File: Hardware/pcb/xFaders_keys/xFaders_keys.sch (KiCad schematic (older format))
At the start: 76 parts, among them J1 Conn_02x10_Odd_Even, SW1 SW_Push, SW10 SW_Push, SW11 SW_Push, SW12 SW_Push, SW13 SW_Push, SW14 SW_Push, SW15 SW_Push, SW16 SW_Push, SW17 SW_Push, SW18 SW_Push, SW19 SW_Push, SW2 SW_Push, SW20 SW_Push, SW21 SW_Push, SW22 SW_Push, SW23 SW_Push, SW24 SW_Push, SW25 SW_Push, SW26 SW_Push, SW27 SW_Push, SW28 SW_Push, SW29 SW_Push, SW3 SW_Push, SW30 SW_Push, SW31 SW_Push, SW32 SW_Push, SW33 SW_Push, SW34 SW_Push, SW35 SW_Push, SW36 SW_Push, SW37 SW_Push, SW38 SW_Push, SW39 SW_Push, SW4 SW_Push, SW40 SW_Push, SW41 SW_Push, SW42 SW_Push, SW43 SW_Push, SW44 SW_Push, SW45 SW_Push, SW5 SW_Push, SW6 SW_Push, SW7 SW_Push, SW8 SW_Push, SW9 SW_Push

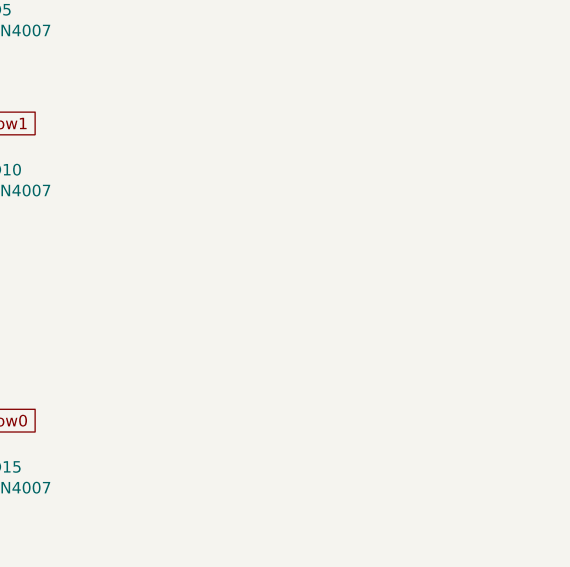
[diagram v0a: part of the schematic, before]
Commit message: Add kicad library for SK6812 MINI-E RGB LEDs
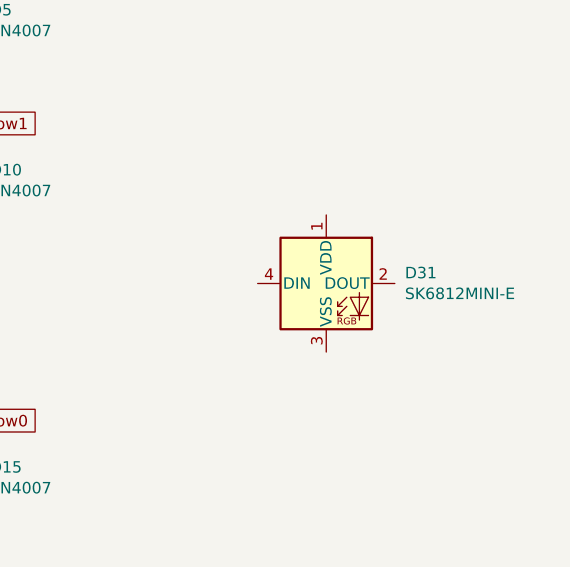
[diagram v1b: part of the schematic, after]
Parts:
- added D31: SK6812MINI-E, kicad-keyboard-parts:MX_SK6812MINI-E, symbol kicad-keyboard-parts:SK6812MINI-E
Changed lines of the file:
@@
 EESchema Schematic File Version 4
-LIBS:xFaders_keys-cache
 EELAYER 30 0
 EELAYER END
@@
 Wire Wire Line
 	6900 6000 6900 5900
+$Comp
+L kicad-keyboard-parts:SK6812MINI-E D31
+U 1 1 6025F252
+P 8450 2500
+F 0 "D31" H 8794 2546 50  0000 L CNN
+F 1 "SK6812MINI-E" H 8794 2455 50  0000 L CNN
+F 2 "kicad-keyboard-parts:MX_SK6812MINI-E" H 8500 2200 50  0001 L TNN
+F 3 "https://cdn-shop.adafruit.com/product-files/2686/SK6812MINI_REV.01-1-2.pdf" H 8550 2125 50  0001 L TNN
+	1    8450 2500
+	1    0    0    -1
+$EndComp
 $EndSCHEMATC

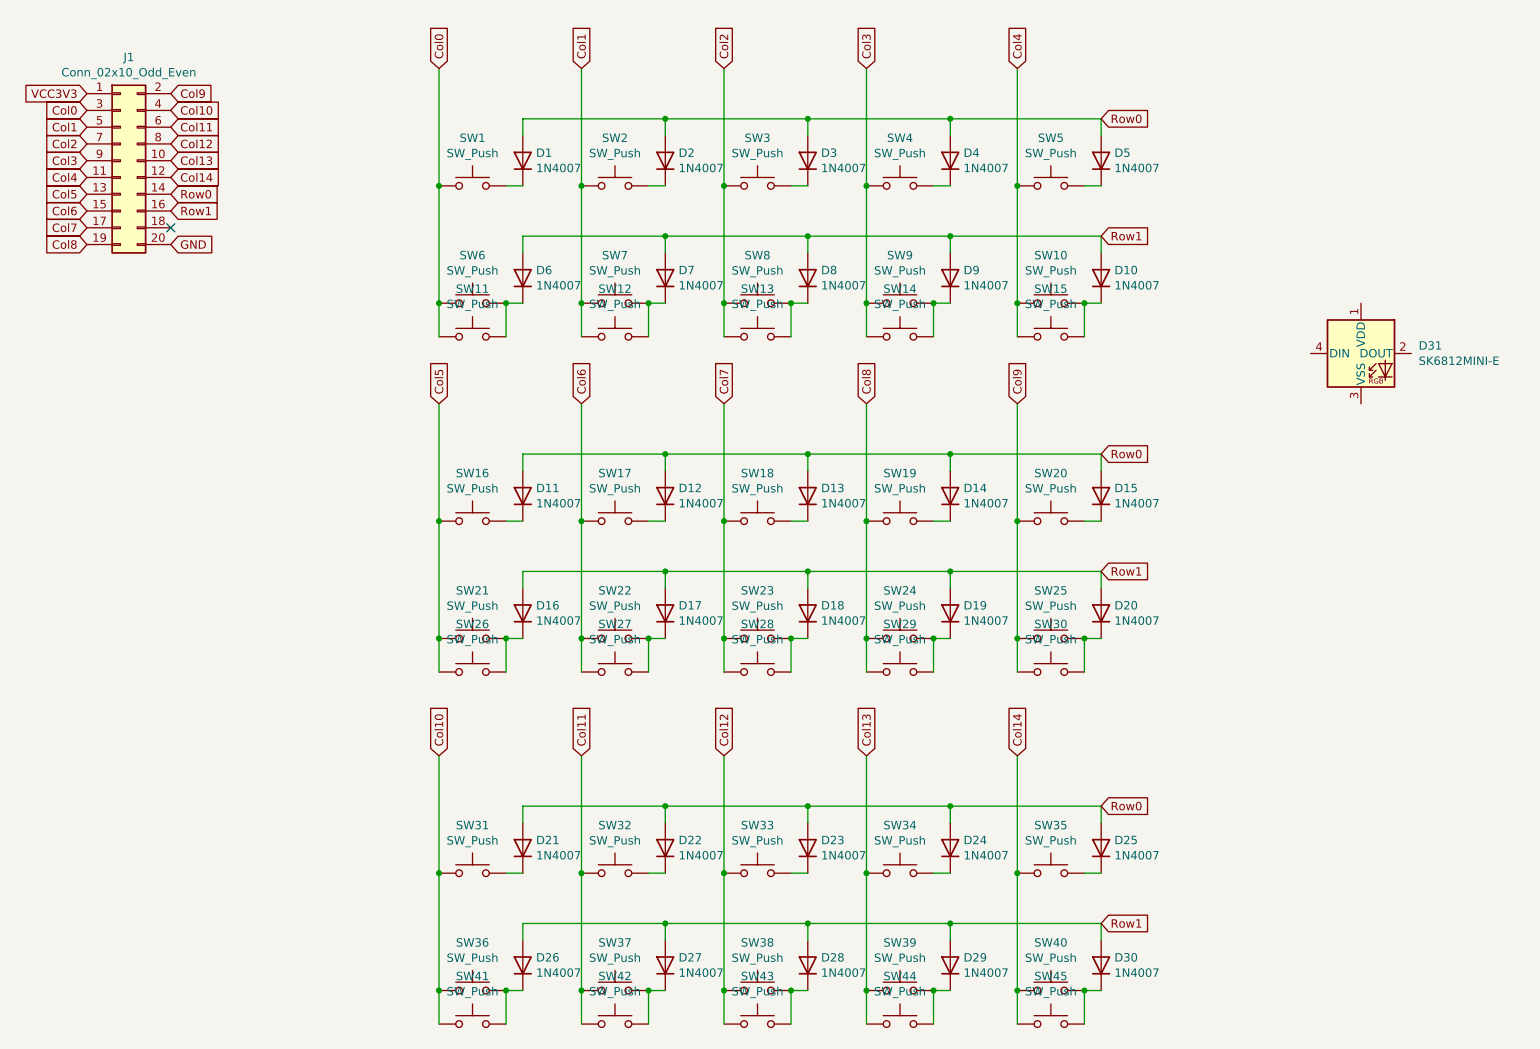
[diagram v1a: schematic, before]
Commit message: Add RGB LEDs and capacitors to Schema and PCB
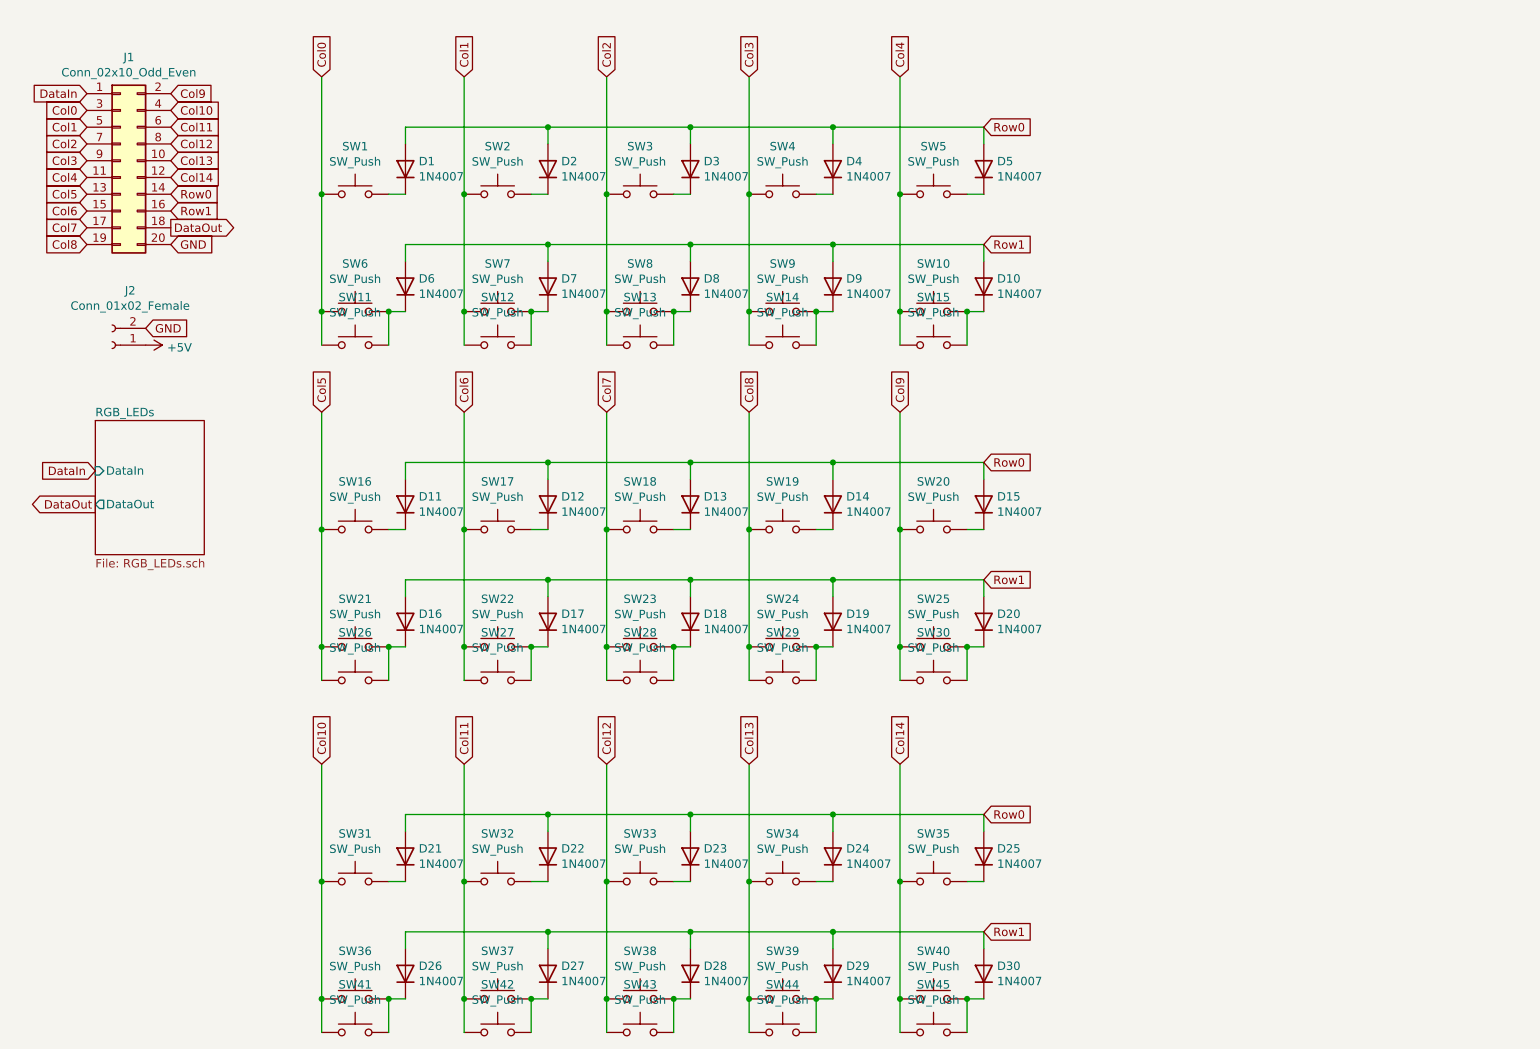
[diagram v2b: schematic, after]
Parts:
- removed D31: SK6812MINI-E, kicad-keyboard-parts:MX_SK6812MINI-E, symbol kicad-keyboard-parts:SK6812MINI-E
- added J2: Conn_01x02_Female, Connector_PinHeader_2.54mm:PinHeader_1x02_P2.54mm_Vertical, symbol Connector:Conn_01x02_Female
- D1, D10, D11, D12, D13, D14, D15, D16, D17, D18, D19, D2, D20, D21, D22, D23, D24, D25, D26, D27, D28, D29, D3, D30, D4, D5, D6, D7, D8, D9: footprint Diode_THT:D_DO-41_SOD81_P10.16mm_Horizontal -> Diode_THT:D_DO-35_SOD27_P10.16mm_Horizontal
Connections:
- net GND: now also J2.2 (Pin_2)
- net DataOut: now reaches J1.18 (Pin_18)
- net VCC3V3 renamed DataIn
- new net +5V: J2.1 (Pin_1)
- no-connect marks 1 -> 0
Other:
- moved on the sheet: D1, D10, D11, D12, D13, D14, D15, D16, D17, D18, D19, D2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

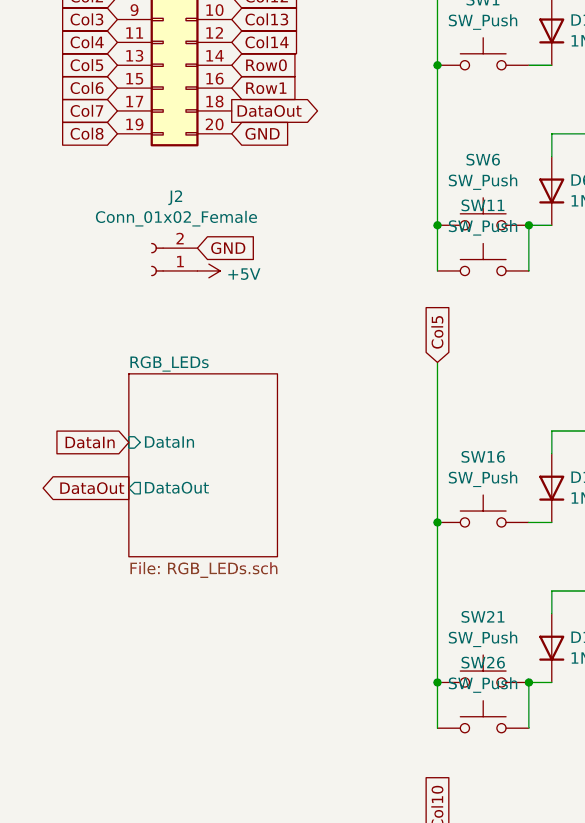
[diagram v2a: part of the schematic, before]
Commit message: Update PCB for new RGB LEDs and 5V power supply
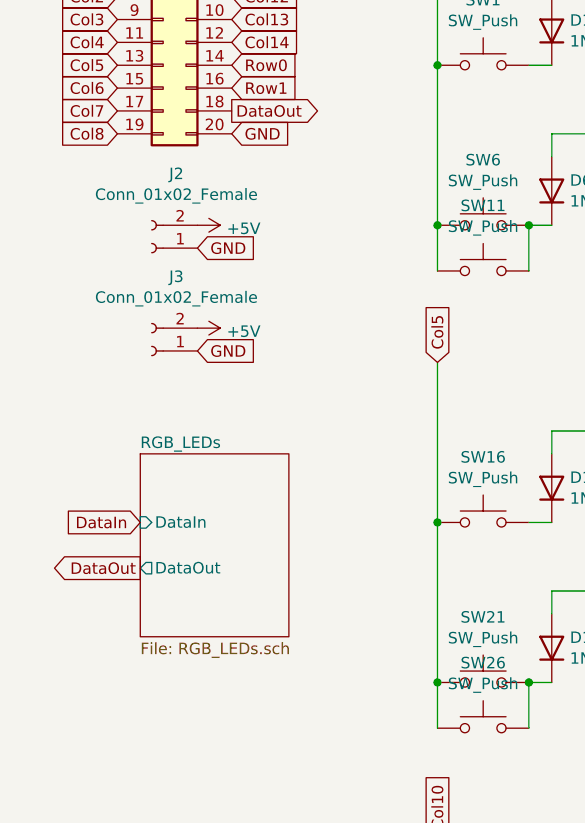
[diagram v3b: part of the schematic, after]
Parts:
- added J3: Conn_01x02_Female, Connector_PinHeader_2.54mm:PinHeader_1x02_P2.54mm_Vertical, symbol Connector:Conn_01x02_Female
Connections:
- net +5V: now also J2.2 (Pin_2), J3.2 (Pin_2); no longer J2.1 (Pin_1)
- net GND: now also J2.1 (Pin_1), J3.1 (Pin_1); no longer J2.2 (Pin_2)
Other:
- moved on the sheet: J2
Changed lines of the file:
@@
 Wire Wire Line
 	6200 6050 6200 5950
-$Sheet
-S 900  2900 650  800
-U 602D74FD
-F0 "RGB_LEDs" 50
-F1 "RGB_LEDs.sch" 50
-F2 "DataIn" I L 900 3200 50
-F3 "DataOut" O L 900 3400 50
-$EndSheet
 $Comp
 L Connector:Conn_01x02_Female J2
 U 1 1 605C87E4
-P 1000 2450
-F 0 "J2" H 892 2125 50  0000 C CNN
-F 1 "Conn_01x02_Female" H 892 2216 50  0000 C CNN
-F 2 "Connector_PinHeader_2.54mm:PinHeader_1x02_P2.54mm_Vertical" H 1000 2450 50  0001 C CNN
-F 3 "~" H 1000 2450 50  0001 C CNN
-	1    1000 2450
+P 1000 2350
+F 0 "J2" H 892 2025 50  0000 C CNN
+F 1 "Conn_01x02_Female" H 892 2116 50  0000 C CNN
+F 2 "Connector_PinHeader_2.54mm:PinHeader_1x02_P2.54mm_Vertical" H 1000 2350 50  0001 C CNN
+F 3 "~" H 1000 2350 50  0001 C CNN
+	1    1000 2350
 	-1   0    0    1
 $EndComp
@@
 L power:+5V #PWR025
 U 1 1 605CA370
-P 1200 2450
-F 0 "#PWR025" H 1200 2300 50  0001 C CNN
-F 1 "+5V" V 1215 2578 50  0000 L CNN
-F 2 "" H 1200 2450 50  0001 C CNN
-F 3 "" H 1200 2450 50  0001 C CNN
-	1    1200 2450
+P 1200 2250
+F 0 "#PWR025" H 1200 2100 50  0001 C CNN
+F 1 "+5V" V 1215 2378 50  0000 L CNN
+F 2 "" H 1200 2250 50  0001 C CNN
+F 3 "" H 1200 2250 50  0001 C CNN
+	1    1200 2250
 	0    1    1    0
 $EndComp
@@
 Text GLabel 1350 1750 2    50   Output ~ 0
 DataOut
-Text GLabel 900  3200 0    50   Input ~ 0
+Text GLabel 950  3550 0    50   Input ~ 0
 DataIn
-Text GLabel 900  3400 0    50   Output ~ 0
+Text GLabel 950  3750 0    50   Output ~ 0
 DataOut
+$Comp
+L Connector:Conn_01x02_Female J3
+U 1 1 6064A5CA
+P 1000 2800
+F 0 "J3" H 892 2475 50  0000 C CNN
+F 1 "Conn_01x02_Female" H 892 2566 50  0000 C CNN
+F 2 "Connector_PinHeader_2.54mm:PinHeader_1x02_P2.54mm_Vertical" H 1000 2800 50  0001 C CNN
+F 3 "~" H 1000 2800 50  0001 C CNN
+	1    1000 2800
+	-1   0    0    1
+$EndComp
+Text GLabel 1200 2800 2    50   Input ~ 0
+GND
+$Comp
+L power:+5V #PWR013
+U 1 1 6064A5D1
+P 1200 2700
+F 0 "#PWR013" H 1200 2550 50  0001 C CNN
+F 1 "+5V" V 1215 2828 50  0000 L CNN
+F 2 "" H 1200 2700 50  0001 C CNN
+F 3 "" H 1200 2700 50  0001 C CNN
+	1    1200 2700
+	0    1    1    0
+$EndComp
+$Sheet
+S 950  3250 650  800
+U 602D74FD
+F0 "RGB_LEDs" 50
+F1 "RGB_LEDs.sch" 50
+F2 "DataIn" I L 950 3550 50
+F3 "DataOut" O L 950 3750 50
+$EndSheet
 $EndSCHEMATC
